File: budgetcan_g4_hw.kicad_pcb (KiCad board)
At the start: 4 copper layers, 76.2 x 38.1 mm, 96 parts, among them IC1 M74VHC1GT66DTT1G, IC2 M74VHC1GT66DTT1G, IC3 M74VHC1GT66DTT1G, J1 USB_C_Receptacle_USB2.0, J3 20021511-00014T4LF, J4 Conn_01x02, J5 348260124, U1 AP22804AW5, U12 TJA1021T, U14 TPS2116DRLR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

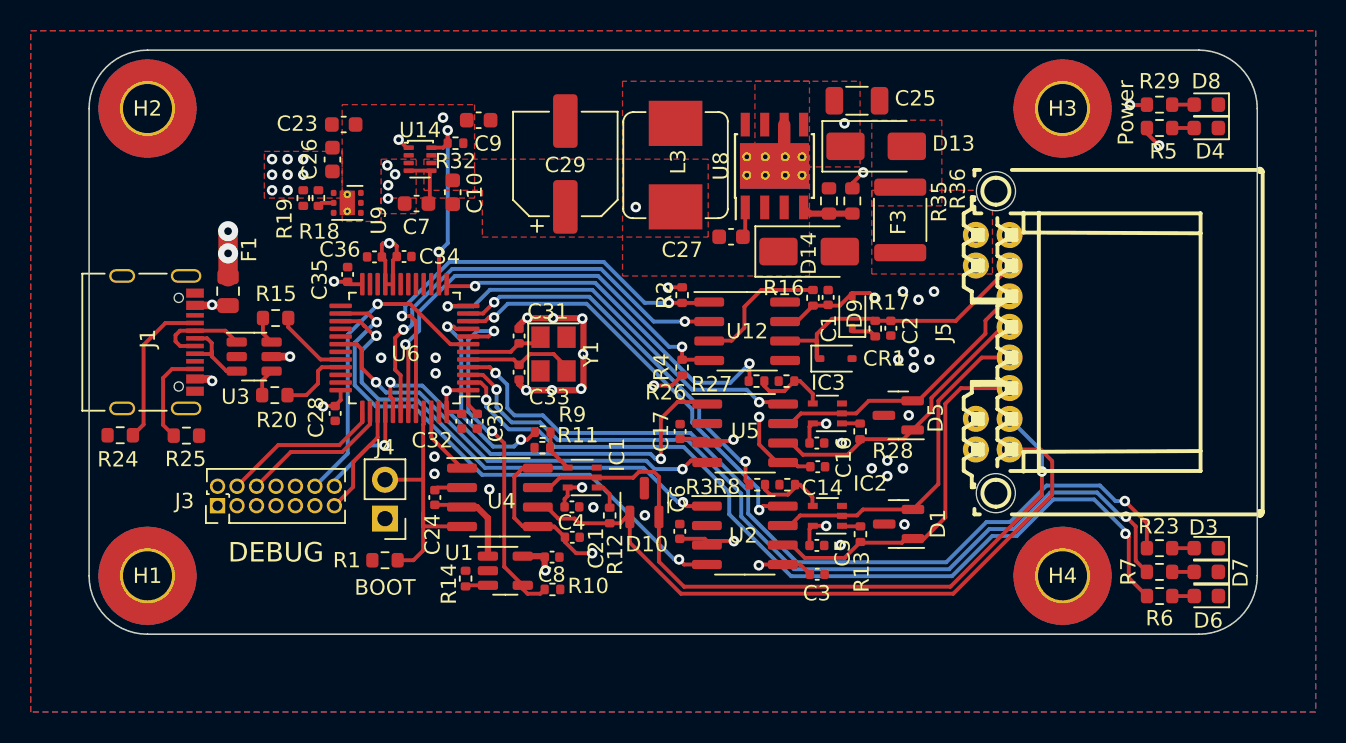
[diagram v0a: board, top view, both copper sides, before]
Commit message: Fix incorrect connection of the 3.3V regulator feedback resistors
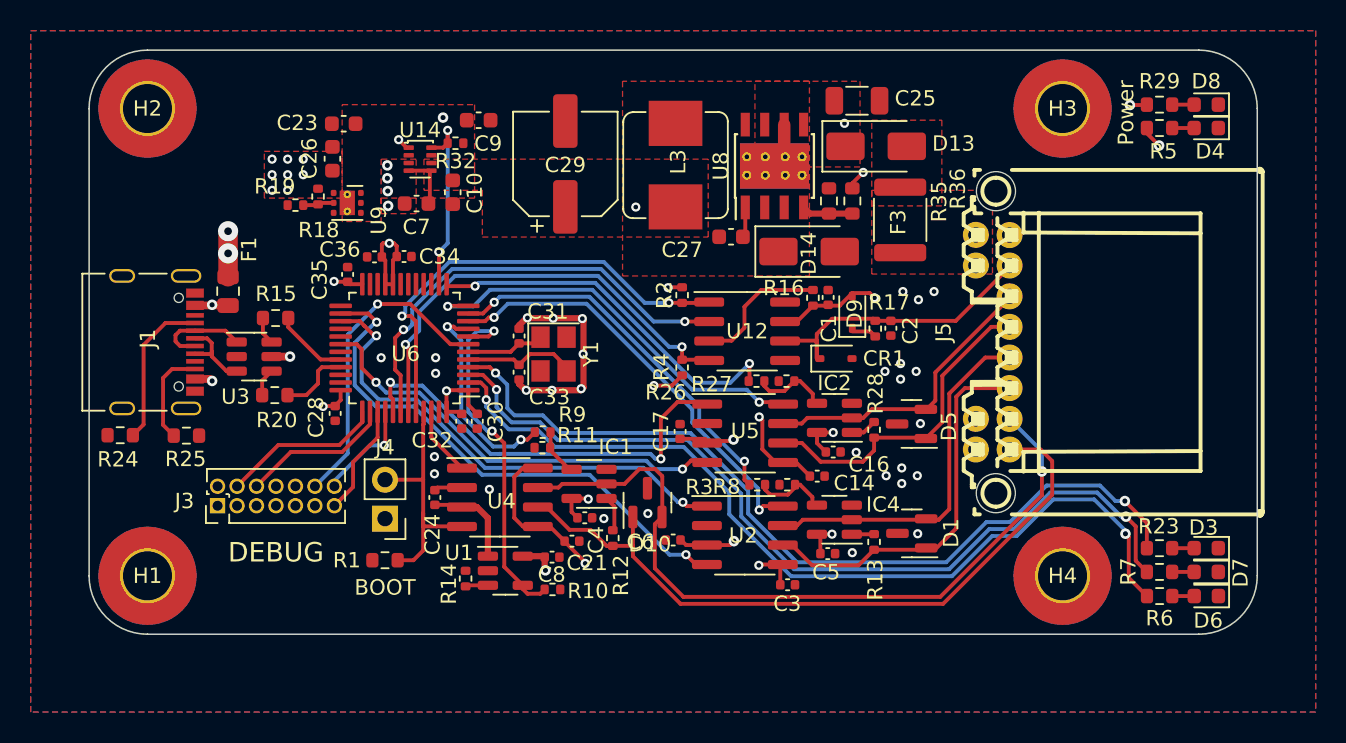
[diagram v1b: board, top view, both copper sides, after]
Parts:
- removed IC3: M74VHC1GT66DTT1G, Package_TO_SOT_SMD:SOT-353_SC-70-5
- added IC4: SN74LVC1G66DBVR, Package_TO_SOT_SMD:SOT-23-5, F.Cu at (161.6, 106.8)
- IC1, IC2: value M74VHC1GT66DTT1G -> SN74LVC1G66DBVR; footprint Package_TO_SOT_SMD:SOT-353_SC-70-5 -> Package_TO_SOT_SMD:SOT-23-5
- R18: value 20k -> 100k
- R19: value 100k -> 20k
- moved IC2 6.41 mm to (161.7, 100.2)
- moved C3 2.05 mm to (158.6, 111.1)
- moved R12 1.49 mm to (147.2, 108.0)
- moved C16 1.22 mm to (161.6, 102.4)
- moved C4 1.10 mm to (145.4, 106.7)
- moved D1 1.06 mm to (166.7, 107.7)
- moved D5 1.03 mm to (166.7, 100.6)
- moved R13 1.02 mm to (164.2, 108.3)
- moved R28 0.92 mm to (164.2, 101.0)
- moved C5 0.89 mm to (161.2, 109.0)
- moved C6 0.71 mm to (151.1, 108.2), turned to 0 degrees
- moved R19 0.68 mm to (126.5, 86.3), turned to 180 degrees
- moved C14 0.61 mm to (160.5, 104.0)
- moved IC1 0.61 mm to (145.6, 104.5)
- moved C21 0.26 mm to (144.5, 108.2)
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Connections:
- IC2 pad 2: HSCAN2_H -> HSCAN3_H
- R13 pad 1: Net-(IC2-A) -> Net-(IC4-A)
- R19 pad 1: +3V3 -> Net-(U9-FB)
- R26 pad 2: Net-(IC3-C) -> Net-(IC2-C)
- R27 pad 1: Net-(IC3-C) -> Net-(IC2-C)
- R28 pad 1: Net-(IC3-A) -> Net-(IC2-A)
- R3 pad 2: Net-(IC2-C) -> Net-(IC4-C)
- R8 pad 1: Net-(IC2-C) -> Net-(IC4-C)
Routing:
- net Net-(IC3-C): track 4.86 -> 0.00 mm
- net Net-(IC4-C): track 0.00 -> 4.82 mm
- net HSCAN3_L: track 19.9 -> 22.4 mm
- net HSCAN2_L: track 23.4 -> 25.2 mm
- net HSCAN1_H: track 48.0 -> 49.6 mm
- net HSCAN1_L: track 45.3 -> 46.8 mm
- net Net-(IC4-A): track 0.00 -> 1.46 mm
- net HSCAN2_H: track 22.5 -> 23.8 mm
- net Net-(IC3-A): track 1.19 -> 0.00 mm
- net Net-(U9-FB): track 1.07 -> 2.04 mm
- net HSCAN3_H: track 18.3 -> 19.2 mm

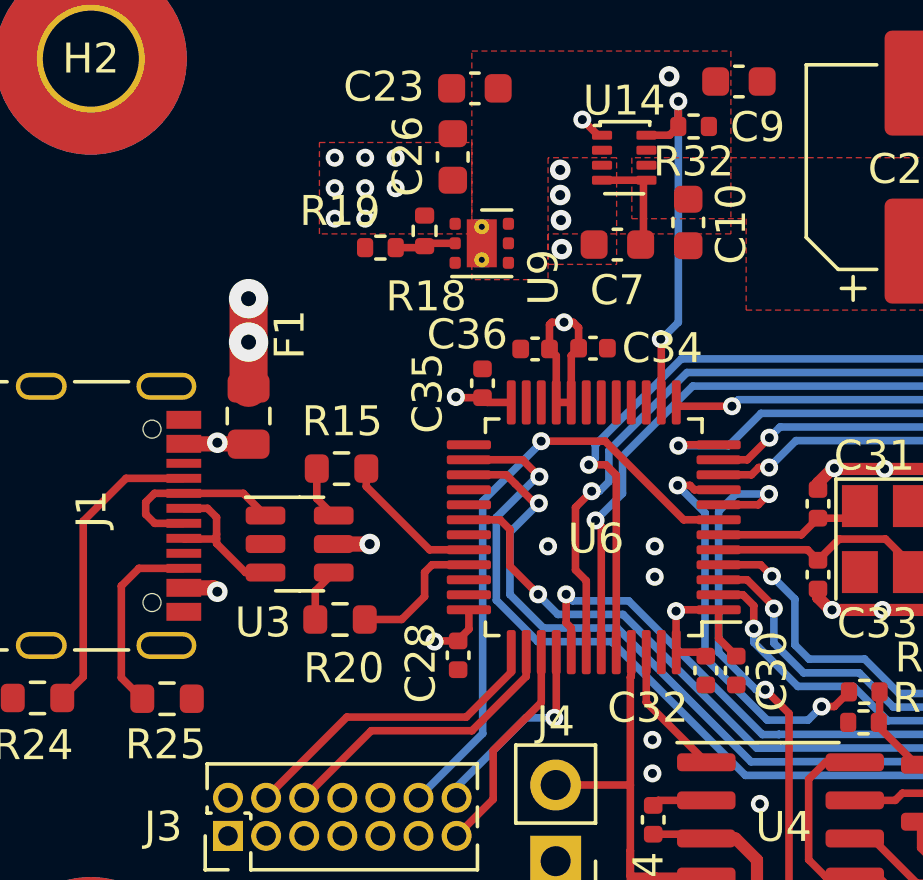
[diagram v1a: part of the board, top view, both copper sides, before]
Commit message: Update to KiCad 8 and fix USB pinouts
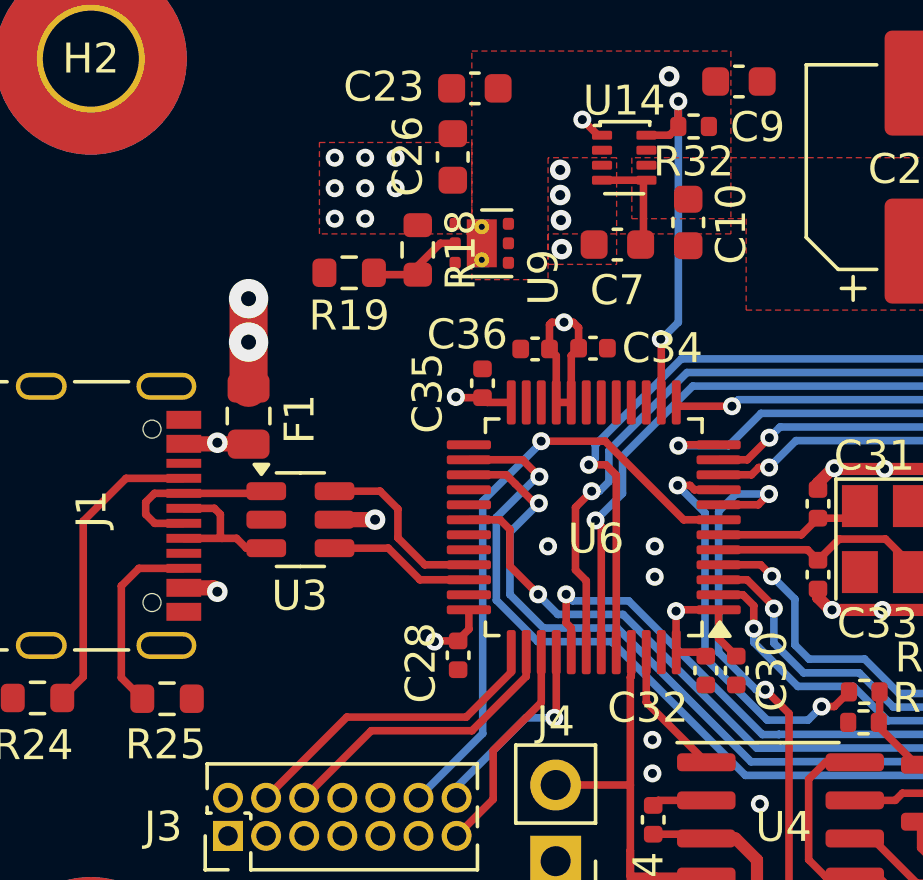
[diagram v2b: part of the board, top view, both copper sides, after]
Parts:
- removed R15, R20: 0R, Resistor_SMD:R_0603_1608Metric
- R18, R19: footprint Resistor_SMD:R_0402_1005Metric -> Resistor_SMD:R_0603_1608Metric
- moved R19 1.34 mm to (125.5, 87.1)
- moved U3 0.81 mm to (123.8, 95.4)
- moved R18 0.67 mm to (127.7, 86.4)
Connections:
- U3 pad 4: Net-(R20-Pad1) -> USB_P
- U3 pad 6: Net-(R15-Pad2) -> USB_N
- U6 pad 32: USB_N -> unconnected-(U6-PA10-Pad32)
- U6 pad 33: USB_P -> USB_N
- U6 pad 34: unconnected-(U6-PA12-Pad34) -> USB_P
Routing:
- net Net-(R20-Pad1): track 1.82 -> 0.00 mm
- net Net-(R15-Pad2): track 1.80 -> 0.00 mm
- net Net-(U9-FB): track 2.04 -> 3.34 mm
- net USB_N: track 4.89 -> 6.06 mm
- net USB_5V: track 27.6 -> 27.0 mm

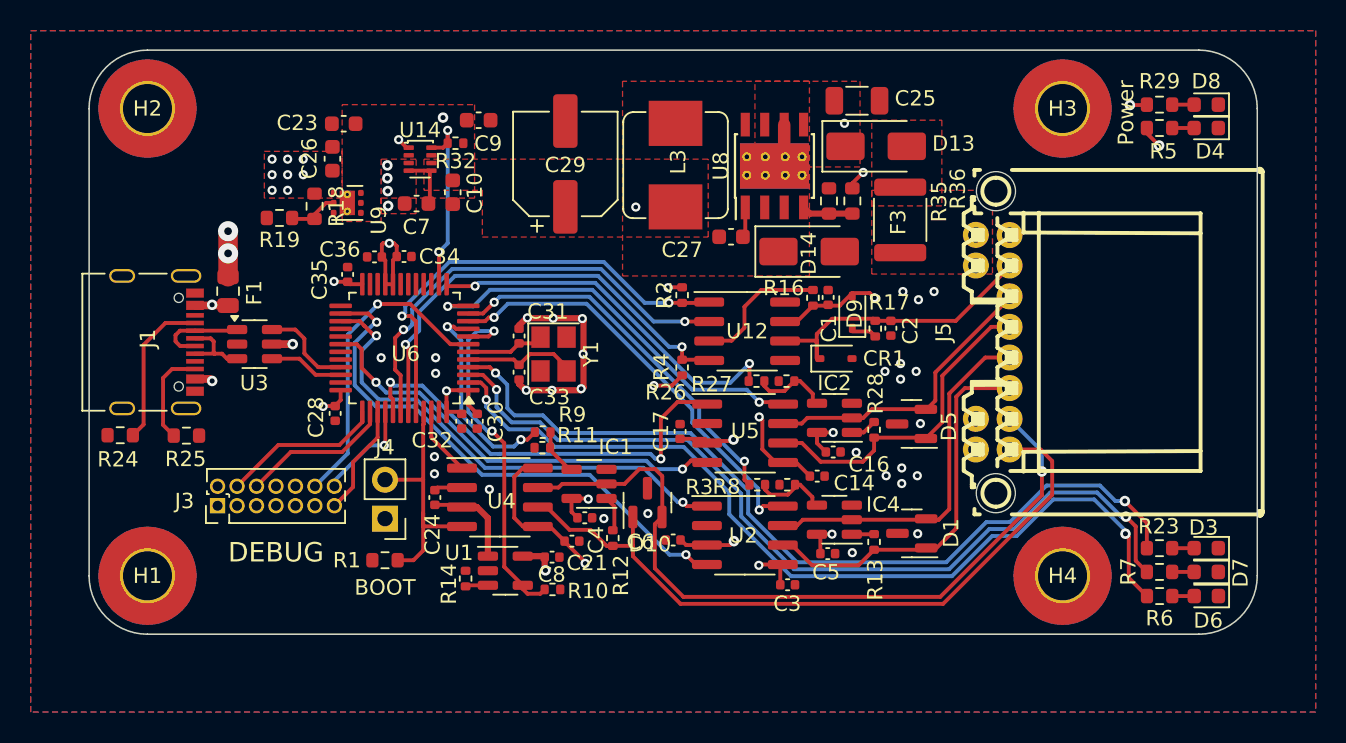
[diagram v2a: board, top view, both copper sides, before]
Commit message: Changes to fix issues found with prototype
- Fixed the power feed for FDCAN1 from switching the 5V feed (VCC) to the 3.3V feed (VIO)
- Changed the XTAL to 8Mhz
- Added a SW controlled master switch for LIN
- Changed the boot selector to a button switch
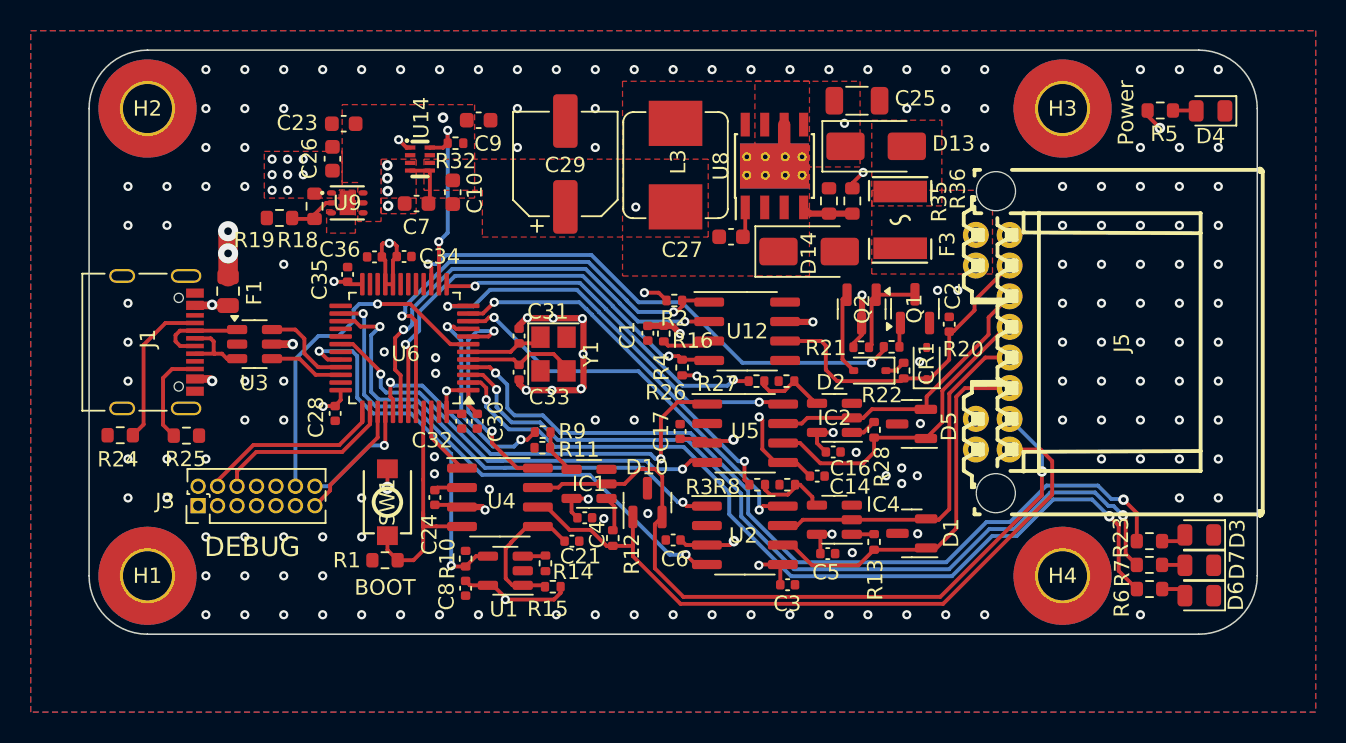
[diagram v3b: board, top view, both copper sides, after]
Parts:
- removed D8: LED_RED, LED_SMD:LED_0603_1608Metric
- removed D9: ‎1N4448WX-TP‎, Diode_SMD:D_SOD-323
- removed J4: Conn_01x02, Connector_PinHeader_2.54mm:PinHeader_1x02_P2.54mm_Vertical
- removed R17: 1k, Resistor_SMD:R_0402_1005Metric
- removed R29: 2.2k, Resistor_SMD:R_0603_1608Metric
- added D2: ‎1N4448WX-TP‎, Diode_SMD:D_SOD-323, F.Cu at (164.0, 97.1)
- added Q1: 2N7002, Package_TO_SOT_SMD:SOT-23, F.Cu at (163.4, 93.1)
- added Q2: MMBT3904, Package_TO_SOT_SMD:SOT-23, F.Cu at (166.9, 93.1)
- added R15: 0R, Resistor_SMD:R_0402_1005Metric, F.Cu at (143.3, 111.2)
- added R20: 1k, Resistor_SMD:R_0402_1005Metric, F.Cu at (165.4, 95.6)
- added R21: 10k, Resistor_SMD:R_0402_1005Metric, F.Cu at (163.4, 95.6)
- added R22: 1k, Resistor_SMD:R_0402_1005Metric, F.Cu at (166.2, 97.1)
- added SW1: TS-1088-AR02016, jlcpcb_parts:SW-SMD_L3.9-W3.0-P4.45, F.Cu at (132.5, 105.7)
- D3, D4, D6, D7: footprint LED_SMD:LED_0603_1608Metric -> LED_SMD:LED_0805_2012Metric
- F3: footprint Fuse:Fuse_1812_4532Metric -> jlcpcb_parts:F1812
- J5: footprint kicad_lceda:CONN-TH_348260124 -> jlcpcb_parts:CONN-TH_348260124
- U14: footprint Package_TO_SOT_SMD:SOT-583-8 -> jlcpcb_parts:SOT-583-8_L2.1-W1.6-P0.50-LS1.6-BL
- U9: footprint Package_SON:WSON-6-1EP_2x2mm_P0.65mm_EP1x1.6mm_ThermalVias -> jlcpcb_parts:WSON-6_L2.0-W2.0-P0.65-TL-EP
- Y1: value 12Mhz -> 8Mhz
- moved C1 12.0 mm to (149.5, 94.7), turned to -90 degrees
- moved R16 10.0 mm to (150.5, 94.7), turned to 90 degrees
- moved R10 6.01 mm to (137.6, 109.4), turned to 90 degrees
- moved C8 5.99 mm to (137.6, 111.3), turned to -90 degrees
- moved CR1 5.93 mm to (167.7, 96.6), turned to 90 degrees
- moved R14 5.30 mm to (142.8, 109.7), turned to -90 degrees
- moved C2 3.82 mm to (169.1, 94.1), turned to 90 degrees
- moved J3 1.27 mm to (120.1, 105.9)
- moved D4 1.15 mm to (186.2, 80.2)
- moved R5 1.14 mm to (182.9, 80.1)
- moved D3 0.98 mm to (185.4, 107.8)
- moved R6 0.80 mm to (182.2, 111.4)
- moved R23 0.80 mm to (182.2, 108.2)
- moved R7 0.80 mm to (182.2, 109.8)
- moved D7 0.63 mm to (185.4, 109.8)
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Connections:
- net LIN1_NSLP renamed LIN1_NSLEEP
- net LIN_1 renamed LIN1
- C21 pad 1: +3V3 -> FDCAN1_VIO
- C24 pad 2: FDCAN1_VCC -> +5V
- C8 pad 1: +5V -> +3V3
- R10 pad 1: FDCAN1_SLEEP_EN -> FDCAN1_VIO_EN
- U1 pad 1: FDCAN1_VCC -> FDCAN1_VIO
- U1 pad 4: FDCAN1_SLEEP_EN -> FDCAN1_VIO_EN
- U1 pad 5: +5V -> +3V3
- U4 pad 3: FDCAN1_VCC -> +5V
- U4 pad 5: +3V3 -> FDCAN1_VIO
- U4 pad 8: +3V3 -> FDCAN1_SLEEP_EN
- U6 pad 15: unconnected-(U6-PA7-Pad15) -> LIN1_MASTER_SW
- U6 pad 32: unconnected-(U6-PA10-Pad32) -> FDCAN1_VIO_EN
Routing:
- net LIN1_MASTER_SW: track 0.00 -> 35.2 mm, vias 0 -> 2
- net FDCAN1_VIO_EN: track 0.00 -> 24.7 mm, vias 0 -> 2
- net FDCAN1_VIO: track 0.00 -> 9.63 mm
- net FDCAN1_SLEEP_EN: track 23.3 -> 15.0 mm
- net +12V: track 40.2 -> 33.5 mm, vias 3 -> 4
- net FDCAN1_VCC: track 6.31 -> 0.00 mm
- net Net-(Q1-G): track 0.00 -> 6.16 mm
- net Net-(U12-~{WAKE}): track 9.09 -> 3.20 mm
- net Net-(D2-A): track 0.00 -> 5.38 mm
- net +3V3: track 47.9 -> 45.7 mm, vias 21 -> 22
- net NRST: track 20.6 -> 22.6 mm
- net LIN1: track 19.3 -> 21.2 mm
- net SWCLK: track 9.89 -> 11.7 mm
- net Net-(D9-K): track 1.63 -> 0.00 mm
- net Net-(Q2-B): track 0.00 -> 1.58 mm
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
